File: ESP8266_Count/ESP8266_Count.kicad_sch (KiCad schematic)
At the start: 26 parts, among them J1 PMG, J2 String1, J3 OLED, SW1 SW_Push, U1 AMS1117-3.3, U2 AMS1117-5.0, U3 ESP-12E, U4 74AHCT1G125, U5 ACS706xLC-05C

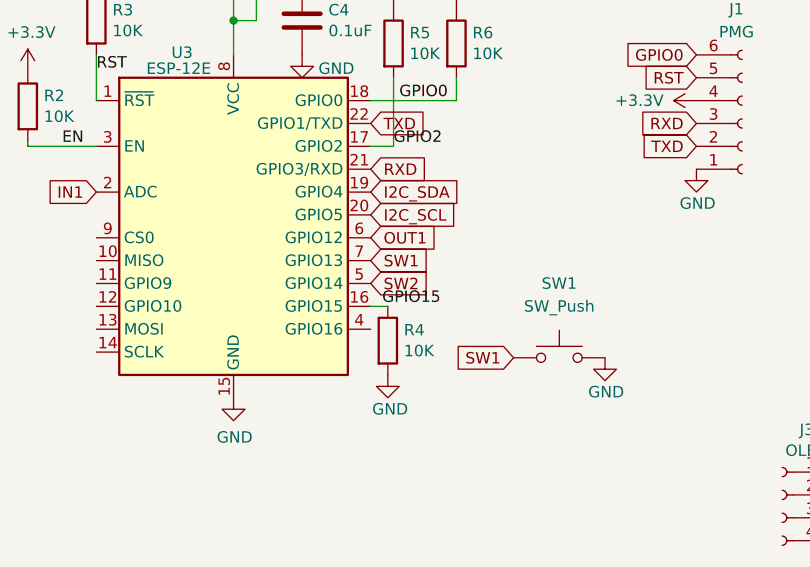
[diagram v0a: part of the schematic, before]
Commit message: added dmx to stepper
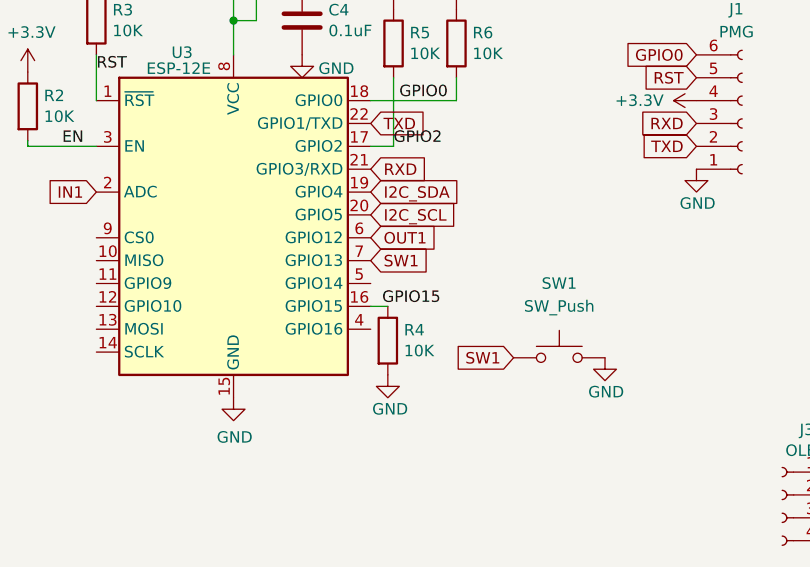
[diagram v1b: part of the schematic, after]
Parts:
- C1: footprint Capacitor_SMD:C_0805_2012Metric_Pad1.18x1.45mm_HandSolder -> Capacitor_SMD:C_1206_3216Metric_Pad1.33x1.80mm_HandSolder; LCSC (none) -> C15008
- SW1: LCSC (none) -> C2834918
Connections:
- net SW2: no longer names the net of U3.5 (GPIO14)
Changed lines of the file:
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@@
-    )
-  )
-  (global_label "SW2" (shape input) (at 150.495 111.76 0) (fields_autoplaced)
-    (effects (font (size 1.27 1.27)) (justify left))
-    (property "Intersheet References" "${INTERSHEET_REFS}" (id 0) (at 156.7786 111.6806 0)
-      (effects (font (size 1.27 1.27)) (justify left) hide)
     )
   )
@@
       (effects (font (size 1.27 1.27)) (justify left))
     )
-    (property "Footprint" "Capacitor_SMD:C_0805_2012Metric_Pad1.18x1.45mm_HandSolder" (id 2) (at 60.7822 118.11 0)
+    (property "Footprint" "Capacitor_SMD:C_1206_3216Metric_Pad1.33x1.80mm_HandSolder" (id 2) (at 60.7822 118.11 0)
       (effects (font (size 1.27 1.27)) hide)
     )
     (property "Datasheet" "~" (id 3) (at 59.817 114.3 0)
+      (effects (font (size 1.27 1.27)) hide)
+    )
+    (property "LCSC" "C15008" (id 4) (at 59.817 114.3 0)
       (effects (font (size 1.27 1.27)) hide)
     )
@@
     )
     (property "Datasheet" "~" (id 3) (at 171.45 114.935 0)
+      (effects (font (size 1.27 1.27)) hide)
+    )
+    (property "LCSC" "C2834918" (id 4) (at 171.45 120.015 0)
       (effects (font (size 1.27 1.27)) hide)
     )
@@
     )
     (path "/4d6388b4-2317-4509-b037-4da89ad19e54"
-      (reference "C1") (unit 1) (value "100uF") (footprint "Capacitor_SMD:C_0805_2012Metric_Pad1.18x1.45mm_HandSolder")
+      (reference "C1") (unit 1) (value "100uF") (footprint "Capacitor_SMD:C_1206_3216Metric_Pad1.33x1.80mm_HandSolder")
     )
     (path "/73fd3938-dfa0-41d2-a921-5e7699b41592"
